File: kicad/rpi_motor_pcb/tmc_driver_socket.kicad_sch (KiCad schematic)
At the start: 2 parts, among them J2 ${SHEETNAME}

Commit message: rpi_motor_pcb: 6-axis canbus version
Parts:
- added C5: 100µF 50V, Capacitor_SMD:CP_Elec_6.3x7.7, symbol Device:C_Polarized_Small
- added JP13: MS3, Jumper:SolderJumper-3_P1.3mm_Open_RoundedPad1.0x1.5mm, symbol Jumper:SolderJumper_3_Open
- added JP14: MS2, Jumper:SolderJumper-3_P1.3mm_Open_RoundedPad1.0x1.5mm, symbol Jumper:SolderJumper_3_Open
- added JP15: MS1, Jumper:SolderJumper-3_P1.3mm_Open_RoundedPad1.0x1.5mm, symbol Jumper:SolderJumper_3_Open
- A5: renamed from A3; value MKS_TMC2209 ${SHEETNAME} -> (none)
- renumbered J2 to J7
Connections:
- net +3V3: now also JP13.3 (B), JP14.3 (B), JP15.3 (B)
- net GND: now also C5.2, JP13.1 (A), JP14.1 (A), JP15.1 (A); no longer A5.10 (MS1), A5.11 (MS2)
- net UART: now also A5.14 (NC/CLK)
- net Vin: now also C5.1
- net MS3: now reaches A5.12 (NC/TX)
- net MS3: now also JP13.2 (C)
- net INDEX: no longer names the net of A5.18 (INDEX)
- new net MS1: A5.10 (MS1), JP15.2 (C)
- new net MS2: A5.11 (MS2), JP14.2 (C)
- no-connect marks 2 -> 1

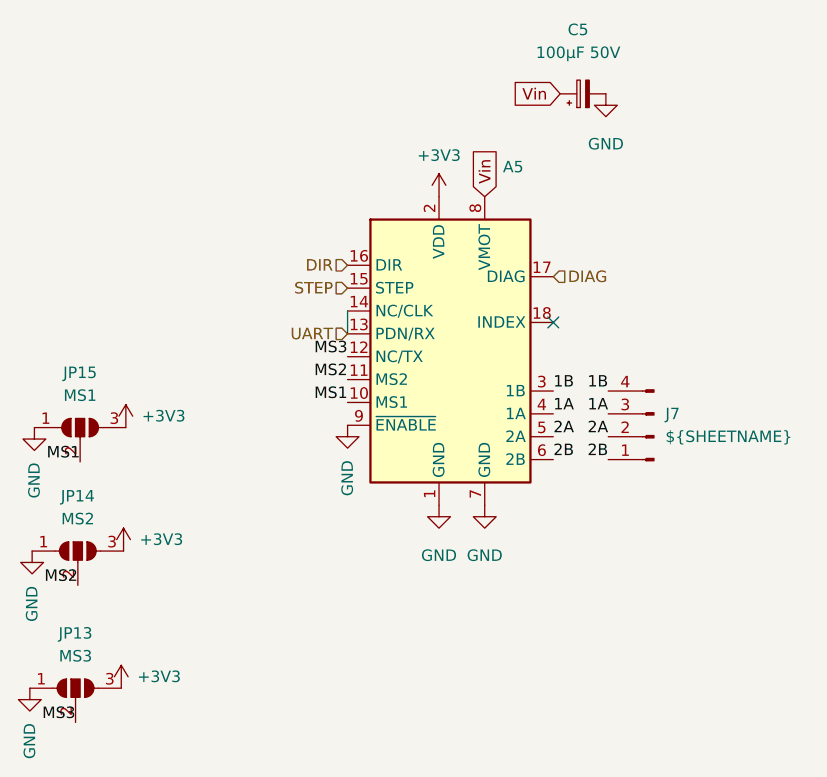
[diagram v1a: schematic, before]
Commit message: rpi_motor_pcb: 6-axis fix diag pin, add en pin
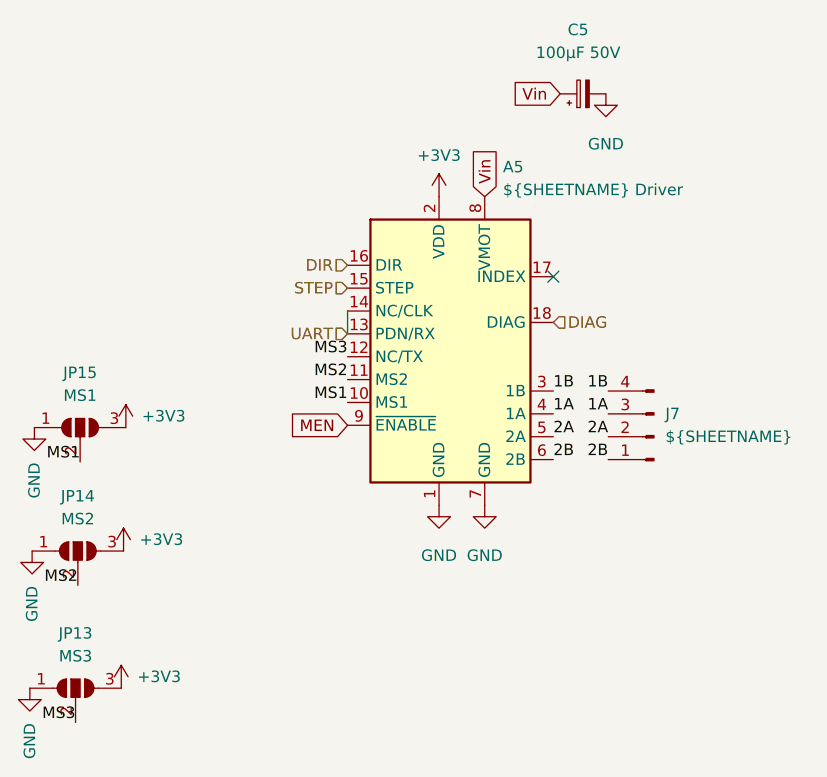
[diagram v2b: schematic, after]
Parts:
- A5: value (none) -> ${SHEETNAME} Driver
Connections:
- net DIAG: now also A5.18 (DIAG); no longer A5.17 (DIAG)
- net GND: no longer A5.9 (~{ENABLE})
- new net MEN: A5.9 (~{ENABLE})
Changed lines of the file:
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@@
 (kicad_sch (version 20211123) (generator eeschema)
   (paper "A4")
-  (no_connect (at 87.63 51.562))
+  (no_connect (at 87.63 46.482))
   (wire (pts (xy 64.77 50.292) (xy 64.77 52.832))
     (stroke (width 0) (type default) (color 0 0 0 0))
@@
     )
   )
+  (global_label "MEN" (shape input) (at 64.77 62.992 180) (fields_autoplaced)
+    (effects (font (size 1.27 1.27)) (justify right))
+    (property "Intersheet References" "${INTERSHEET_REFS}" (id 0) (at 58.4259 62.9126 0)
+      (effects (font (size 1.27 1.27)) (justify right) hide)
+    )
+  )
   (global_label "Vin" (shape input) (at 88.392 26.162 180) (fields_autoplaced)
     (effects (font (size 1.27 1.27)) (justify right))
@@
     (effects (font (size 1.27 1.27)) (justify right))
   )
-  (hierarchical_label "DIAG" (shape input) (at 87.63 46.482 0)
+  (hierarchical_label "DIAG" (shape input) (at 87.63 51.562 0)
     (effects (font (size 1.27 1.27)) (justify left))
   )
@@
       (effects (font (size 1.27 1.27)) (justify left))
     )
-    (property "Value" "" (id 1) (at 82.0294 36.83 0)
+    (property "Value" "${SHEETNAME} Driver" (id 1) (at 82.0294 36.83 0)
       (effects (font (size 1.27 1.27)) (justify left))
     )
@@
       (effects (font (size 1.27 1.27)) hide)
     )
-    (pin "1")
-  )
-  (symbol (lib_id "power:GND") (at 64.77 62.992 0) (unit 1)
-    (in_bom yes) (on_board yes)
-    (property "Reference" "#PWR021" (id 0) (at 64.77 69.342 0)
-      (effects (font (size 1.27 1.27)) hide)
-    )
-    (property "Value" "GND" (id 1) (at 64.77 70.866 90)
-      (effects (font (size 1.27 1.27)) (justify left))
-    )
-    (property "Footprint" "" (id 2) (at 64.77 62.992 0)
-      (effects (font (size 1.27 1.27)) hide)
-    )
-    (property "Datasheet" "" (id 3) (at 64.77 62.992 0)
-      (effects (font (size 1.27 1.27)) hide)
-    )
